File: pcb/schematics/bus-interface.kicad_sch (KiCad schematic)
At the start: 6 parts

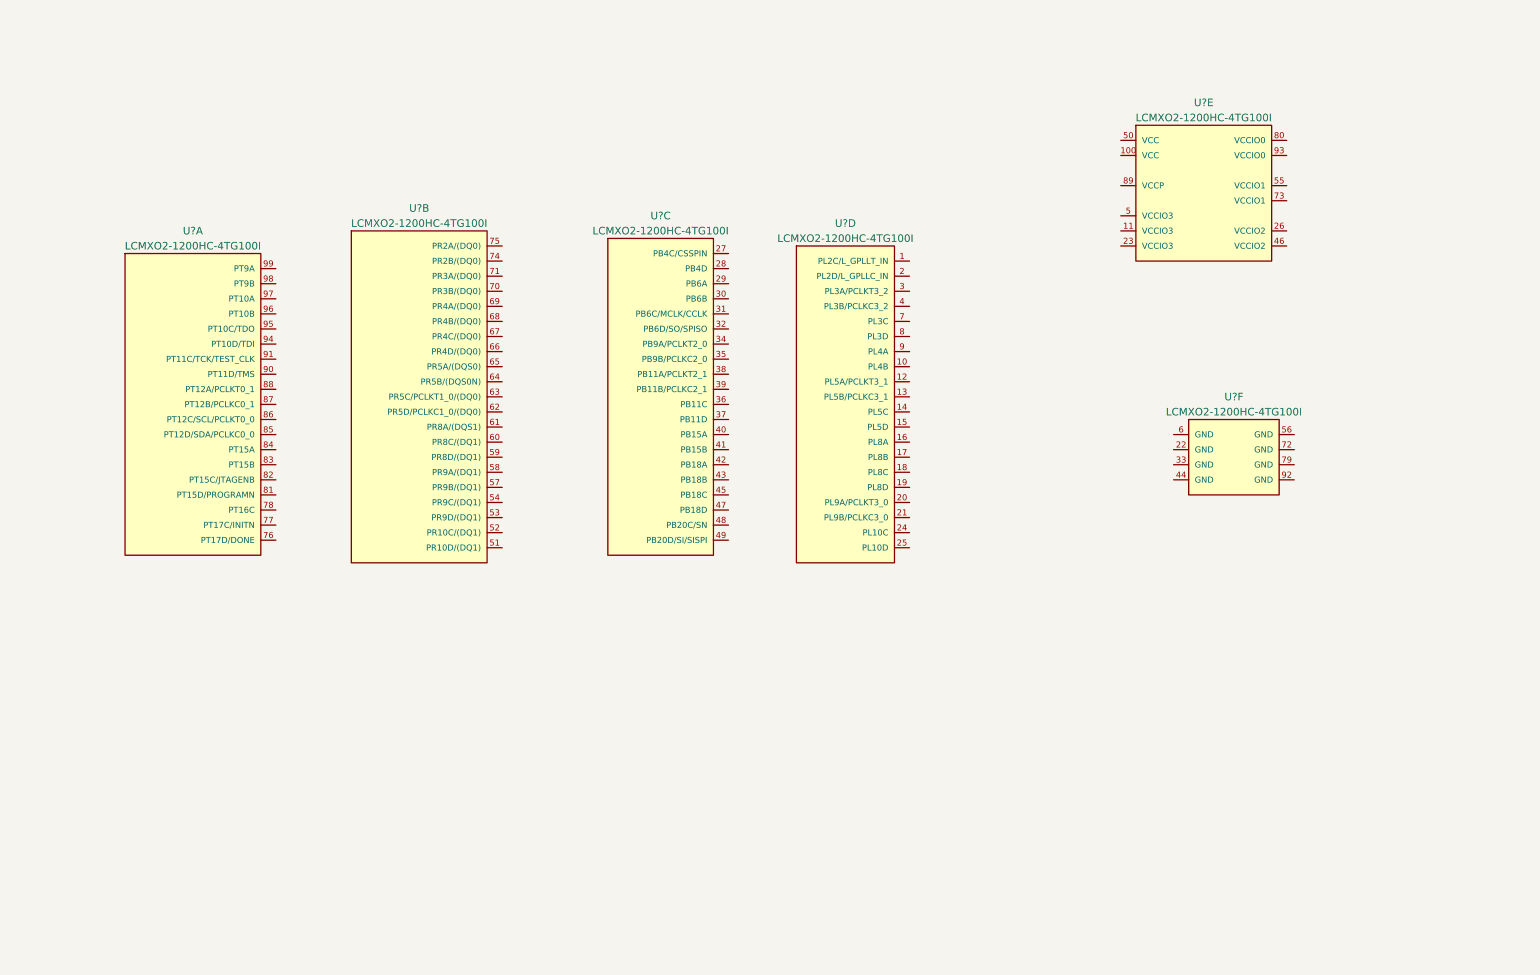
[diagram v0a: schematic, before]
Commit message: add architecture diagramé
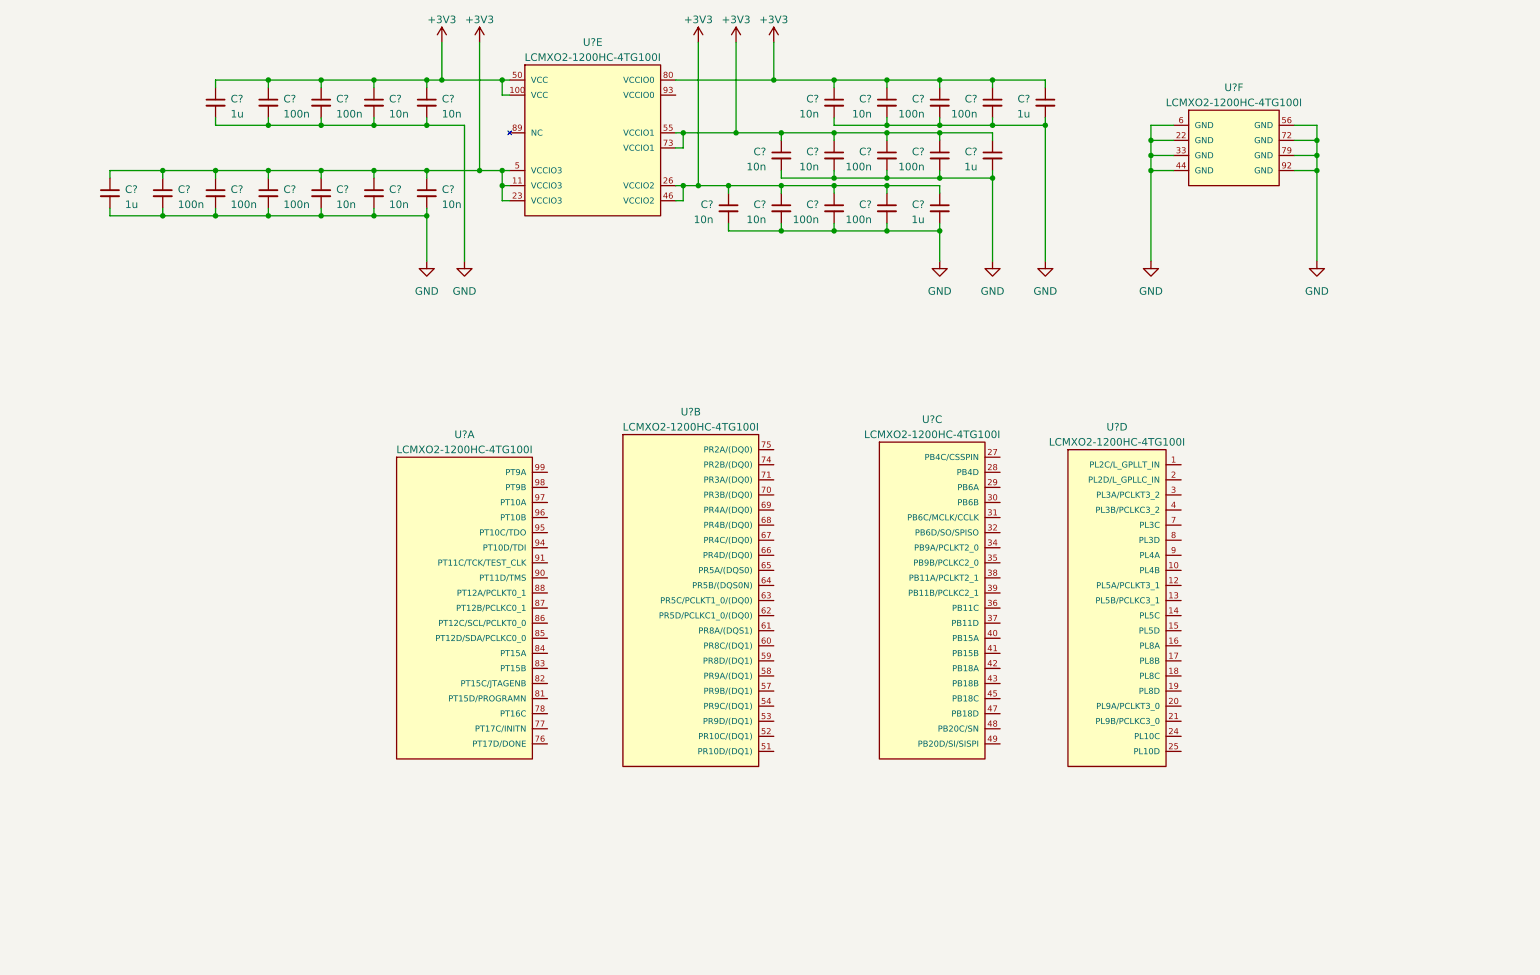
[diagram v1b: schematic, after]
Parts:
- added C? (x5): 1u, symbol Device:C_Small
- added C? (x11): 10n, symbol Device:C_Small
- added C? (x11): 100n, symbol Device:C_Small
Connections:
- net GND: now reaches U?.22 (GND)
- net GND: now also U?.33 (GND), U?.44 (GND), U?.56 (GND), U?.6 (GND), U?.72 (GND), U?.79 (GND), U?.92 (GND), C?.2, C?.2, C?.2, C?.2, C?.2, C?.2, C?.2, C?.2, C?.2, C?.2, C?.2, C?.2, C?.2, C?.2, C?.2, C?.2, C?.2, C?.2, C?.2, C?.2, C?.2, C?.2, C?.2, C?.2, C?.2, C?.2, C?.2
- net +3V3: now reaches U?.100 (VCC)
- net +3V3: now also U?.11 (VCCIO3), U?.23 (VCCIO3), U?.26 (VCCIO2), U?.46 (VCCIO2), U?.5 (VCCIO3), U?.50 (VCC), U?.55 (VCCIO1), U?.73 (VCCIO1), U?.80 (VCCIO0), C?.1, C?.1, C?.1, C?.1, C?.1, C?.1, C?.1, C?.1, C?.1, C?.1, C?.1, C?.1, C?.1, C?.1, C?.1, C?.1, C?.1, C?.1, C?.1, C?.1, C?.1, C?.1, C?.1, C?.1, C?.1, C?.1, C?.1
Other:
- moved on the sheet: U?A, U?B, U?C, U?D, U?F

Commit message: add jtag and spi tag connect to the bus fpga
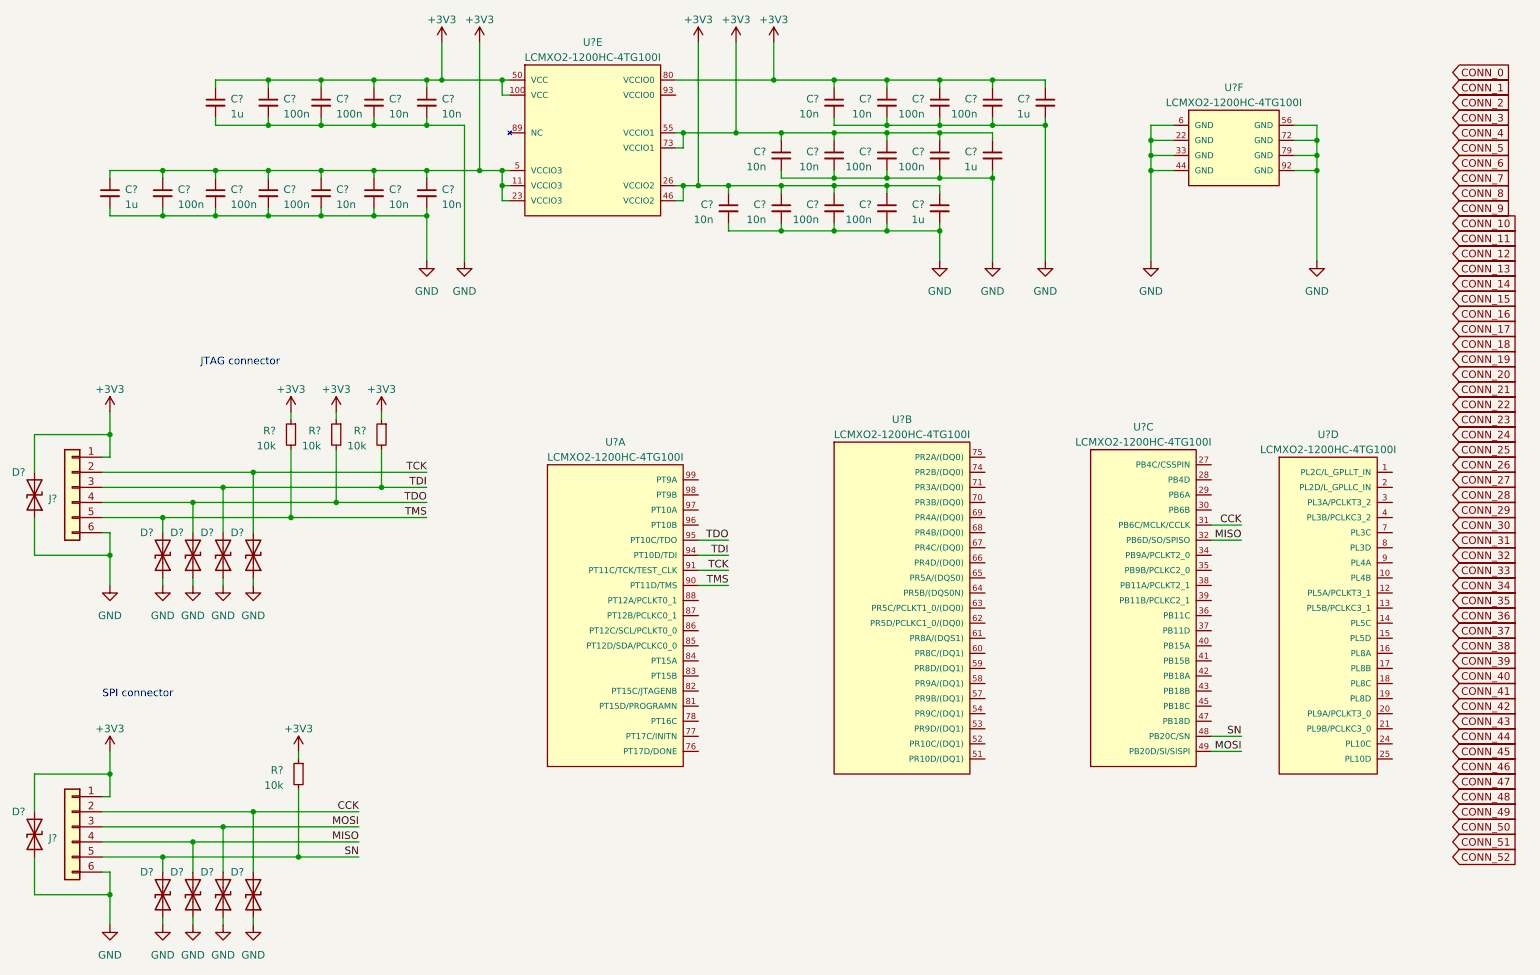
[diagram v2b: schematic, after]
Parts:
- added D? (x10): D_TVS, symbol Device:D_TVS
- added J? (x2): Conn_01x06, symbol Connector_Generic:Conn_01x06
- added R? (x4): 10k, symbol Device:R_Small
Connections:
- net +3V3: now also D?.2 (A2), D?.2 (A2), J?.1 (Pin_1), J?.1 (Pin_1), R?.1, R?.1, R?.1, R?.1
- net GND: now also D?.1 (A1), D?.1 (A1), D?.1 (A1), D?.1 (A1), D?.1 (A1), D?.1 (A1), D?.1 (A1), D?.1 (A1), D?.1 (A1), D?.1 (A1), J?.6 (Pin_6), J?.6 (Pin_6)
- net TMS: now reaches U?.90 (PT11D/TMS)
- net TMS: now also D?.2 (A2), J?.5 (Pin_5), R?.2
- net TCK: now reaches U?.91 (PT11C/TCK/TEST_CLK)
- net TCK: now also D?.2 (A2), J?.2 (Pin_2)
- net TDI: now reaches U?.94 (PT10D/TDI)
- net TDI: now also D?.2 (A2), J?.3 (Pin_3), R?.2
- net TDO: now reaches U?.95 (PT10C/TDO)
- net TDO: now also D?.2 (A2), J?.4 (Pin_4), R?.2
- net CCK: now reaches U?.31 (PB6C/MCLK/CCLK)
- net CCK: now also D?.2 (A2), J?.2 (Pin_2)
- net MISO: now reaches U?.32 (PB6D/SO/SPISO)
- net MISO: now also D?.2 (A2), J?.4 (Pin_4)
- net SN: now reaches U?.48 (PB20C/SN)
- net SN: now also D?.2 (A2), J?.5 (Pin_5), R?.2
- net MOSI: now reaches U?.49 (PB20D/SI/SISPI)
- net MOSI: now also D?.2 (A2), J?.3 (Pin_3)
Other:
- note added: "JTAG connector"
- note added: "SPI connector"
- moved on the sheet: U?A, U?B, U?C, U?D

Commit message: add bypass to the video controller
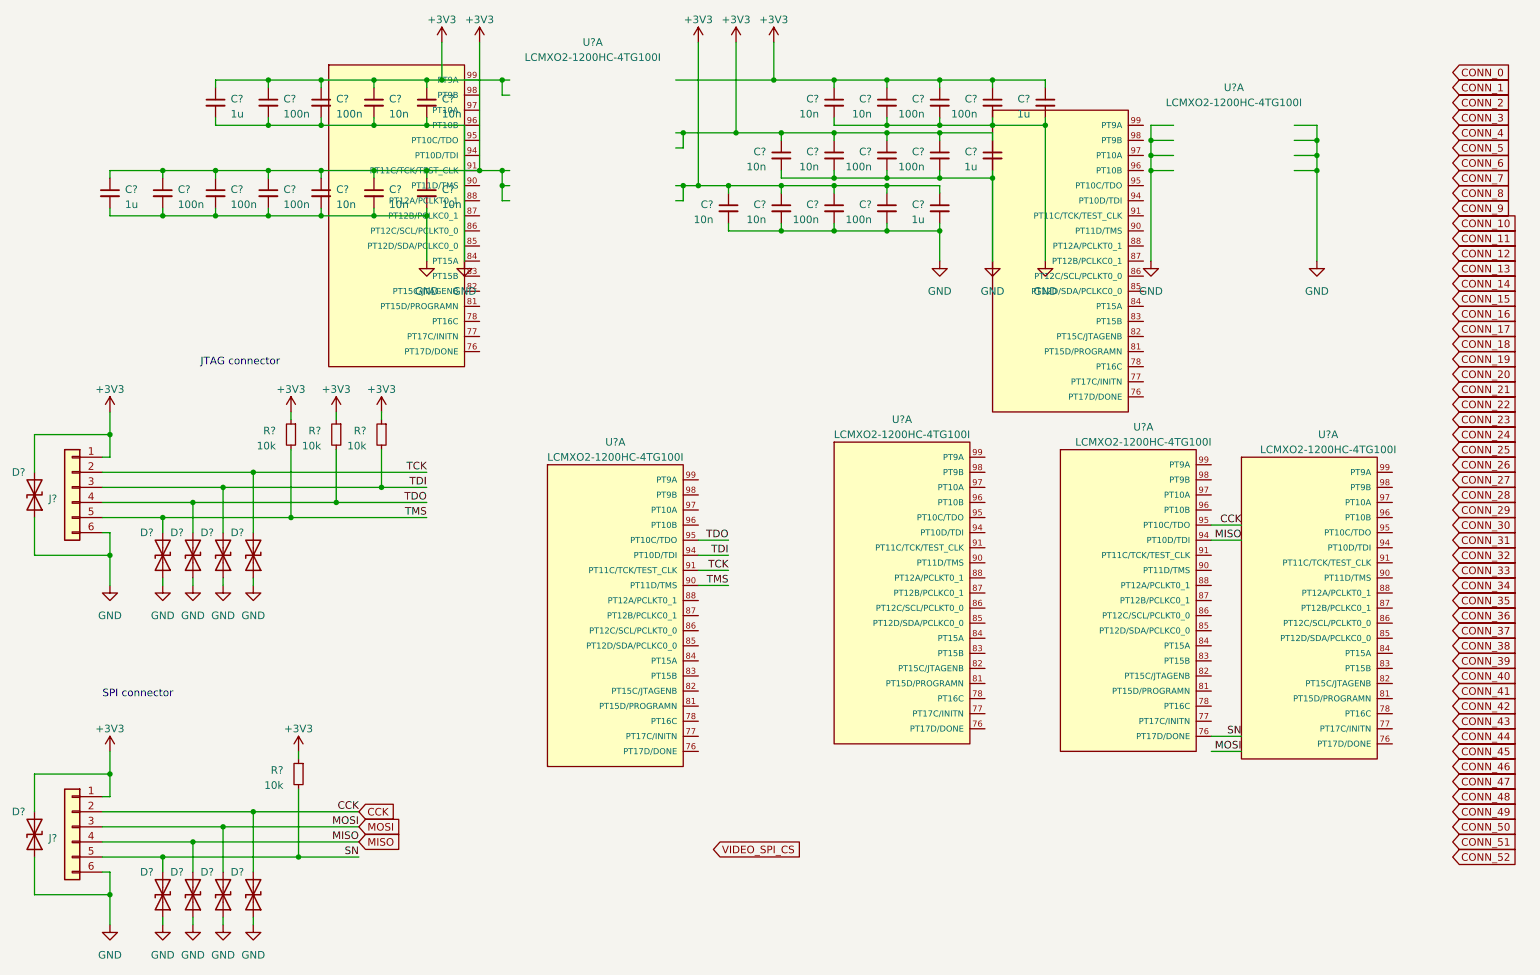
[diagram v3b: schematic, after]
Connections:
- net +3V3: now also U?.91 (PT11C/TCK/TEST_CLK); no longer U?.100 (VCC), U?.11 (VCCIO3), U?.23 (VCCIO3), U?.26 (VCCIO2), U?.46 (VCCIO2), U?.5 (VCCIO3), U?.50 (VCC), U?.55 (VCCIO1), U?.73 (VCCIO1), U?.80 (VCCIO0)
- net CCK: now also U?.95 (PT10C/TDO); no longer U?.31 (PB6C/MCLK/CCLK)
- net GND: no longer U?.22 (GND), U?.33 (GND), U?.44 (GND), U?.56 (GND), U?.6 (GND), U?.72 (GND), U?.79 (GND), U?.92 (GND)
- net MISO: now also U?.94 (PT10D/TDI); no longer U?.32 (PB6D/SO/SPISO)
- net MOSI: no longer U?.49 (PB20D/SI/SISPI)
- net SN: now also U?.76 (PT17D/DONE); no longer U?.48 (PB20C/SN)

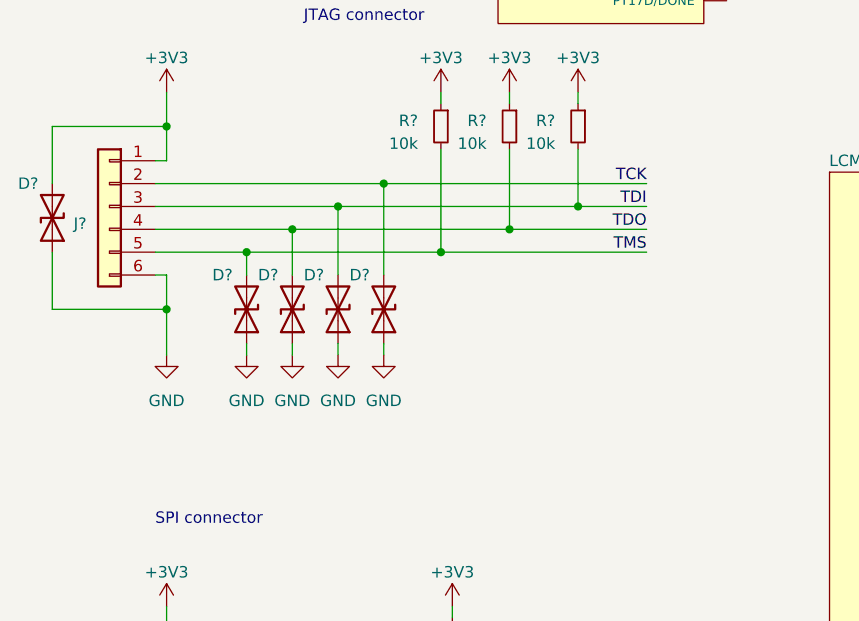
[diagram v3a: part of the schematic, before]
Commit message: add jtag signals to the video controller
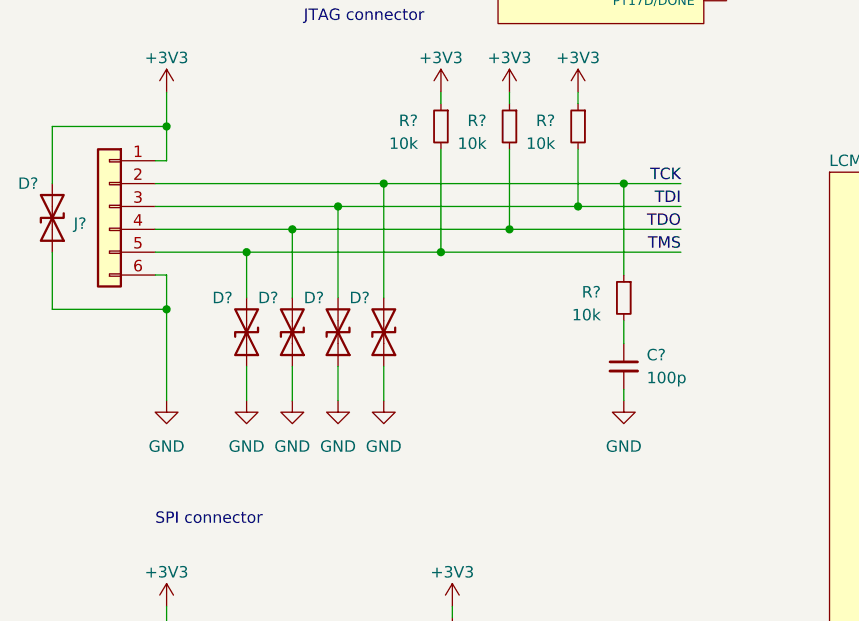
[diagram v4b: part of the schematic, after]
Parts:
- removed D? (x5): D_TVS, symbol Device:D_TVS
- removed J?: Conn_01x06, symbol Connector_Generic:Conn_01x06
- removed R? (x3): 10k, symbol Device:R_Small
- added C?: 100p, symbol Device:C_Small
- added D? (x5): D_TVS, symbol Device:D_TVS
- added J?: Conn_01x06, symbol Connector_Generic:Conn_01x06
- added R? (x4): 10k, symbol Device:R_Small
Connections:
- net +3V3: now also D?.2 (A2), J?.1 (Pin_1), R?.1, R?.1, R?.1
- net GND: now also C?.2, D?.1 (A1), D?.1 (A1), D?.1 (A1), D?.1 (A1), D?.1 (A1), J?.6 (Pin_6)
- net TCK: now also D?.2 (A2), J?.2 (Pin_2), R?.1
- net TDI: now also D?.2 (A2), J?.3 (Pin_3), R?.2
- net TDO: now also D?.2 (A2), J?.4 (Pin_4), R?.2
- net TMS: now also D?.2 (A2), J?.5 (Pin_5), R?.2
- new net: C?.1, R?.2
